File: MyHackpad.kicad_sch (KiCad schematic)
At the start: 15 parts, among them J1 OLED_128x32, SW1 RotaryEncoder_Switch, U1 MOUDLE-SEEEDUINO-XIAO

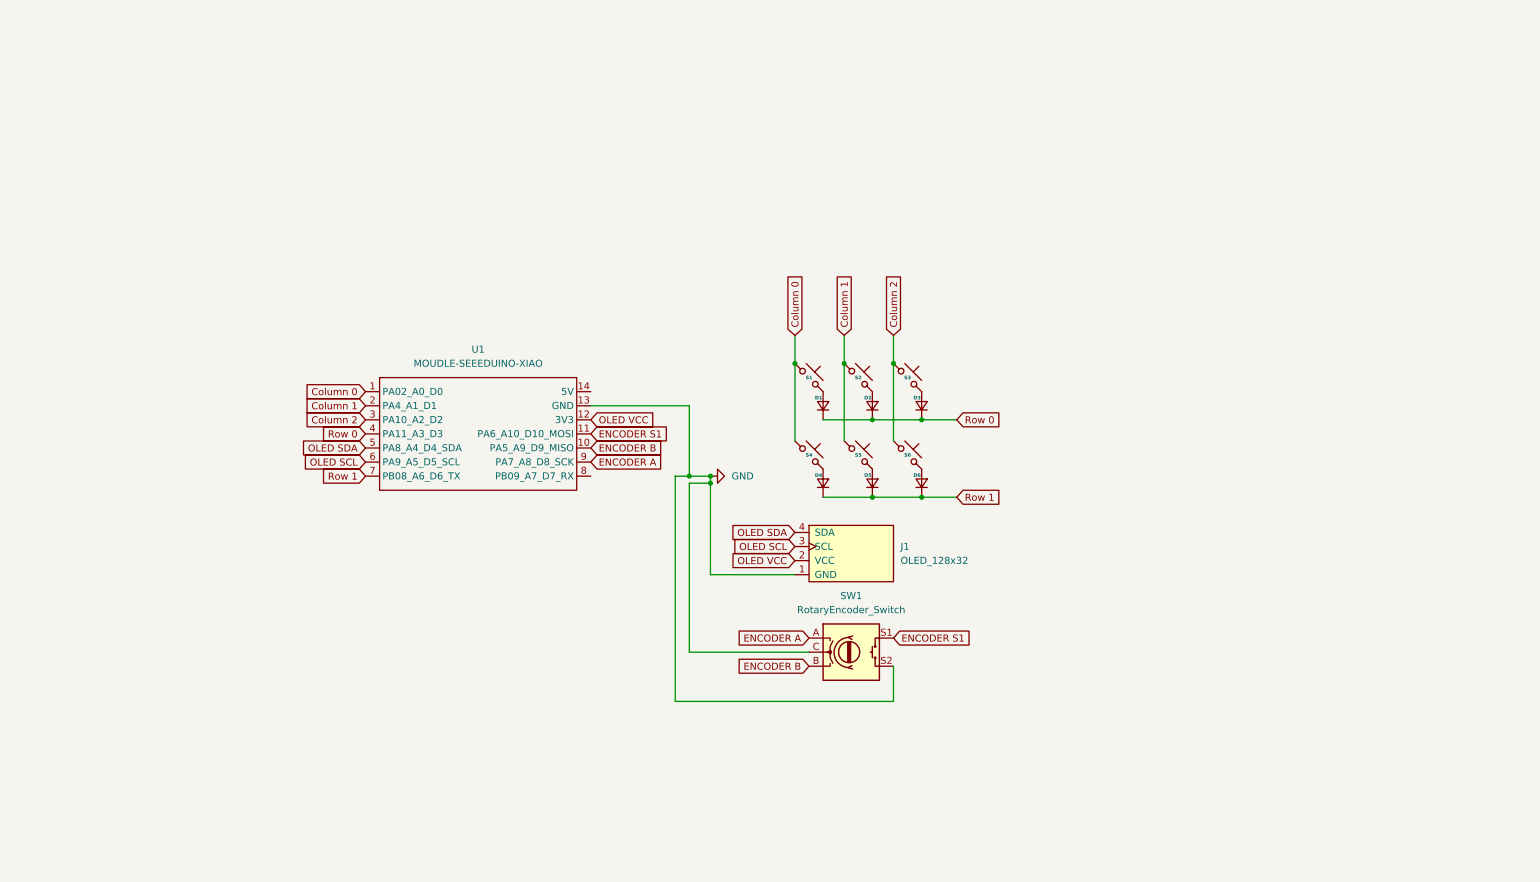
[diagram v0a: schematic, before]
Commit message: Added LEDs to the Schematic
Added some SK6812 MINI-E LEDs to the shcematic and tidied up all connections
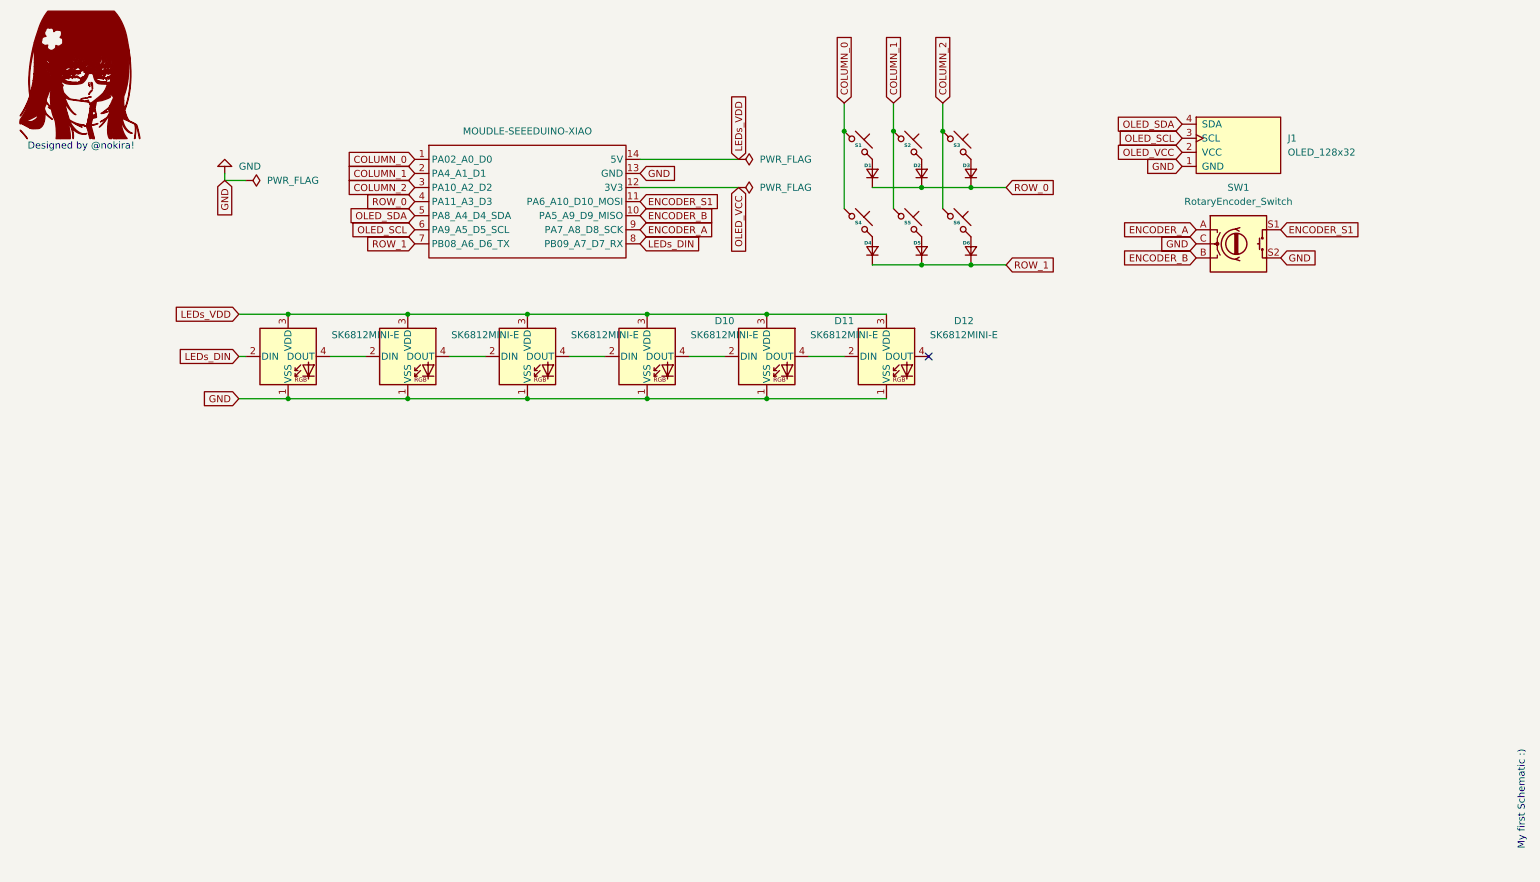
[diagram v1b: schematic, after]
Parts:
- added D10, D11, D12, D7, D8, D9: SK6812MINI-E, LED_SMD:LED_SK6812MINI-E_3.2x2.8mm_P1.5mm_ReverseMount, symbol LED:SK6812MINI-E
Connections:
- net GND: now also D10.1 (VSS), D11.1 (VSS), D12.1 (VSS), D7.1 (VSS), D8.1 (VSS), D9.1 (VSS)
- net LEDs_VDD: now reaches U1.14 (5V)
- net LEDs_VDD: now also D10.3 (VDD), D11.3 (VDD), D12.3 (VDD), D7.3 (VDD), D8.3 (VDD), D9.3 (VDD)
- net LEDs_DIN: now reaches U1.8 (PB09_A7_D7_RX)
- net LEDs_DIN: now also D7.2 (DIN)
- net Column 0 renamed COLUMN_0
- net Column 1 renamed COLUMN_1
- net Column 2 renamed COLUMN_2
- net ENCODER A renamed ENCODER_A
- net ENCODER B renamed ENCODER_B
- net ENCODER S1 renamed ENCODER_S1
- net OLED SCL renamed OLED_SCL
- net OLED SDA renamed OLED_SDA
- net OLED VCC renamed OLED_VCC
- net Row 0 renamed ROW_0
- net Row 1 renamed ROW_1
- new net: D10.2 (DIN), D9.4 (DOUT)
- new net: D10.4 (DOUT), D11.2 (DIN)
- new net: D11.4 (DOUT), D12.2 (DIN)
- new net: D7.4 (DOUT), D8.2 (DIN)
- new net: D8.4 (DOUT), D9.2 (DIN)
- no-connect marks 0 -> 1
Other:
- note added: "Designed by @nokira!"
- note added: "My first Schematic :)"
- moved on the sheet: D1, D2, D3, D4, D5, D6, J1, S1, S2, S3, S4, S5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

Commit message: Placed LEDs correctly on the board
Placed the LEDs thanks to the help found in the Slack channel. Also routed the board from zero because it was quite messy. Now it should be clear :)
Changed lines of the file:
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@@
 			(font
 				(size 1.27 1.27)
+				(color 5 5 5 1)
 			)
 		)
@@
 					(unit 1)
 				)
+			)
+		)
+	)
+	(symbol
+		(lib_id "hackclub_schematic_15x5.2:LOGO")
+		(at 276.86 15.24 0)
+		(unit 1)
+		(body_style 1)
+		(exclude_from_sim no)
+		(in_bom yes)
+		(on_board yes)
+		(in_pos_files yes)
+		(dnp no)
+		(fields_autoplaced yes)
+		(property "Reference" "#G2"
+			(at 276.86 13.2494 0)
+			(hide yes)
+			(show_name no)
+			(do_not_autoplace no)
+			(effects
+				(font
+					(size 1.27 1.27)
+				)
+			)
+		)
+		(property "Value" "LOGO"
+			(at 276.86 17.2306 0)
+			(hide yes)
+			(show_name no)
+			(do_not_autoplace no)
+			(effects
+				(font
+					(size 1.27 1.27)
+				)
+			)
+		)
+		(property "Footprint" ""
+			(at 276.86 15.24 0)
+			(hide yes)
+			(show_name no)
+			(do_not_autoplace no)
+			(effects
+				(font
+					(size 1.27 1.27)
+				)
+			)
+		)
+		(property "Datasheet" ""
+			(at 276.86 15.24 0)
+			(hide yes)
+			(show_name no)
+			(do_not_autoplace no)
+			(effects
+				(font
+					(size 1.27 1.27)
+				)
+			)
+		)
+		(property "Description" ""
+			(at 276.86 15.24 0)
+			(hide yes)
+			(show_name no)
+			(do_not_autoplace no)
+			(effects
+				(font
+					(size 1.27 1.27)
+				)
+			)
+		)
+		(instances
+			(project "MyHackpad"
+				(path "/c8676630-0753-4024-a6c9-20b6cca98ac2"
+					(reference "#G2")
+					(unit 1)
+				)
